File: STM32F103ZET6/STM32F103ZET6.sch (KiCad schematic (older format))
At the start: 74 parts, among them IC1 74HC1G66GW, J1 Conn_01x02, J2 Jack-DC, J3 +5V, J6 USB_B_Micro, Q1 S8050, Q2 S8550, SW1 RESET, SW2 SW_DIP_x01, U1 STM32F103ZETx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

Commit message: STM32F103ZET6.sch
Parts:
- added R14: 10k, symbol Device:R
- C31: value C -> 104
- R12, R13: renamed from R?; value R -> 10k
- U1: value STM32F103ZETx -> STM32F103ZET6
- gave numbers to parts that had none: 2
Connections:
- wire segments 243 -> 246
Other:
- note added: "SWD\n"
- note removed: "STLink"
- moved on the sheet: 1M1, C1, C2, C26, C27, C28, C29, C3, C30, C31, C32, C4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

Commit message: update
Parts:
- added D6, D7: LED, symbol Device:LED
- added R15, R16: 1k, symbol Device:R
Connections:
- net labels added: PB5, PE5
- wire segments 246 -> 255
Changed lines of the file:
@@
 Wire Notes Line
 	18500 4850 18500 500
+$Comp
+L Device:LED D7
+U 1 1 5E75F3EE
+P 14450 5700
+F 0 "D7" H 14443 5916 50  0000 C CNN
+F 1 "LED" H 14443 5825 50  0000 C CNN
+F 2 "" H 14450 5700 50  0001 C CNN
+F 3 "~" H 14450 5700 50  0001 C CNN
+	1    14450 5700
+	1    0    0    -1
+$EndComp
+$Comp
+L Device:LED D6
+U 1 1 5E75ECD8
+P 14450 5300
+F 0 "D6" H 14443 5516 50  0000 C CNN
+F 1 "LED" H 14443 5425 50  0000 C CNN
+F 2 "" H 14450 5300 50  0001 C CNN
+F 3 "~" H 14450 5300 50  0001 C CNN
+	1    14450 5300
+	1    0    0    -1
+$EndComp
+Text Label 14900 5500 0    50   ~ 0
+VCC_3V3
+$Comp
+L Device:R R15
+U 1 1 5E8949B0
+P 13950 5300
+F 0 "R15" V 13743 5300 50  0000 C CNN
+F 1 "1k" V 13834 5300 50  0000 C CNN
+F 2 "" V 13880 5300 50  0001 C CNN
+F 3 "~" H 13950 5300 50  0001 C CNN
+	1    13950 5300
+	0    1    1    0
+$EndComp
+$Comp
+L Device:R R16
+U 1 1 5E8957D1
+P 13950 5700
+F 0 "R16" V 13743 5700 50  0000 C CNN
+F 1 "1k" V 13834 5700 50  0000 C CNN
+F 2 "" V 13880 5700 50  0001 C CNN
+F 3 "~" H 13950 5700 50  0001 C CNN
+	1    13950 5700
+	0    1    1    0
+$EndComp
+Wire Wire Line
+	13800 5300 13600 5300
+Wire Wire Line
+	13800 5700 13600 5700
+Wire Wire Line
+	14100 5700 14300 5700
+Wire Wire Line
+	14100 5300 14300 5300
+Wire Wire Line
+	14600 5300 14700 5300
+Wire Wire Line
+	14700 5300 14700 5500
+Wire Wire Line
+	14700 5700 14600 5700
+Wire Wire Line
+	14700 5500 14900 5500
+Connection ~ 14700 5500
+Wire Wire Line
+	14700 5500 14700 5700
+Text Label 13600 5300 2    50   ~ 0
+PB5
+Text Label 13600 5700 2    50   ~ 0
+PE5
 Wire Bus Line
 	3600 800  3600 2000
@@
 Wire Bus Line
 	1500 3850 5850 3850
+Text Label 11000 6850 1    50   ~ 0
+PB5
+Text Label 14400 9450 3    50   ~ 0
+PE5
 $EndSCHEMATC

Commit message: add led & button
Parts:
- added SW3, SW4, SW5, SW6: SW_Push, symbol Switch:SW_Push
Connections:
- net labels added: +3.3V, PA0, PE2, PE3, PE4
- wire segments 255 -> 266
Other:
- note added: "Button\n"
- note added: "LED\n"
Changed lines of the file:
@@
 	16000 4050 16000 4200
-Wire Notes Line
-	500  6000 13000 6000
 Wire Notes Line
 	13000 500  13000 6000
@@
 Wire Wire Line
 	5350 5400 5500 5400
-Wire Notes Line
-	18500 4850 18500 500
 $Comp
 L Device:LED D7
@@
 Text Label 13600 5700 2    50   ~ 0
 PE5
+Text Label 11000 6850 1    50   ~ 0
+PB5
+Text Label 14400 9450 3    50   ~ 0
+PE5
+Wire Notes Line
+	15500 6000 15500 4850
+Text Notes 15200 5850 0    79   ~ 0
+LED\n
+$Comp
+L Switch:SW_Push SW5
+U 1 1 5E99870A
+P 16950 5500
+F 0 "SW5" V 16950 5750 50  0000 C CNN
+F 1 "SW_Push" V 16850 5700 50  0000 C CNN
+F 2 "" H 16950 5700 50  0001 C CNN
+F 3 "~" H 16950 5700 50  0001 C CNN
+	1    16950 5500
+	0    -1   -1   0
+$EndComp
+$Comp
+L Switch:SW_Push SW3
+U 1 1 5E9982B1
+P 16150 5500
+F 0 "SW3" V 16150 5750 50  0000 C CNN
+F 1 "SW_Push" V 16050 5750 50  0000 C CNN
+F 2 "" H 16150 5700 50  0001 C CNN
+F 3 "~" H 16150 5700 50  0001 C CNN
+	1    16150 5500
+	0    -1   -1   0
+$EndComp
+$Comp
+L Switch:SW_Push SW4
+U 1 1 5E99A749
+P 16550 5500
+F 0 "SW4" V 16550 5750 50  0000 C CNN
+F 1 "SW_Push" V 16450 5700 50  0000 C CNN
+F 2 "" H 16550 5700 50  0001 C CNN
+F 3 "~" H 16550 5700 50  0001 C CNN
+	1    16550 5500
+	0    -1   -1   0
+$EndComp
+$Comp
+L power:GND #PWR018
+U 1 1 5E9FC6A9
+P 16550 5100
+F 0 "#PWR018" H 16550 4850 50  0001 C CNN
+F 1 "GND" H 16450 5050 50  0000 R CNN
+F 2 "" H 16550 5100 50  0001 C CNN
+F 3 "" H 16550 5100 50  0001 C CNN
+	1    16550 5100
+	-1   0    0    1
+$EndComp
+Wire Wire Line
+	16150 5300 16150 5200
+Wire Wire Line
+	16150 5200 16550 5200
+Wire Wire Line
+	16950 5200 16950 5300
+Wire Wire Line
+	16550 5300 16550 5200
+Connection ~ 16550 5200
+Wire Wire Line
+	16550 5200 16950 5200
+Wire Wire Line
+	16550 5100 16550 5200
+Wire Wire Line
+	16150 5700 16150 5850
+Text Label 16150 5850 0    50   ~ 0
+PE2
+Wire Wire Line
+	16550 5700 16550 5850
+Text Label 16550 5850 0    50   ~ 0
+PE3
+Wire Wire Line
+	16950 5700 16950 5850
+Text Label 16950 5850 0    50   ~ 0
+PE4
+$Comp
+L Switch:SW_Push SW6
+U 1 1 5EB5954E
+P 17650 5500
+F 0 "SW6" H 17650 5785 50  0000 C CNN
+F 1 "SW_Push" H 17650 5694 50  0000 C CNN
+F 2 "" H 17650 5700 50  0001 C CNN
+F 3 "~" H 17650 5700 50  0001 C CNN
+	1    17650 5500
+	1    0    0    -1
+$EndComp
+$Comp
+L power:+3.3V #PWR019
+U 1 1 5EB5A9A3
+P 17900 5500
+F 0 "#PWR019" H 17900 5350 50  0001 C CNN
+F 1 "+3.3V" V 17915 5628 50  0000 L CNN
+F 2 "" H 17900 5500 50  0001 C CNN
+F 3 "" H 17900 5500 50  0001 C CNN
+	1    17900 5500
+	0    1    1    0
+$EndComp
+Wire Wire Line
+	17850 5500 17900 5500
+Text Label 17350 5500 2    50   ~ 0
+PA0
+Wire Wire Line
+	17350 5500 17450 5500
+Wire Notes Line
+	18500 500  18500 6000
+Wire Notes Line
+	500  6000 18500 6000
 Wire Bus Line
 	3600 800  3600 2000
@@
 Wire Bus Line
 	1500 3850 5850 3850
-Text Label 11000 6850 1    50   ~ 0
-PB5
-Text Label 14400 9450 3    50   ~ 0
-PE5
+Text Notes 17950 5900 0    79   ~ 0
+Button\n
 $EndSCHEMATC

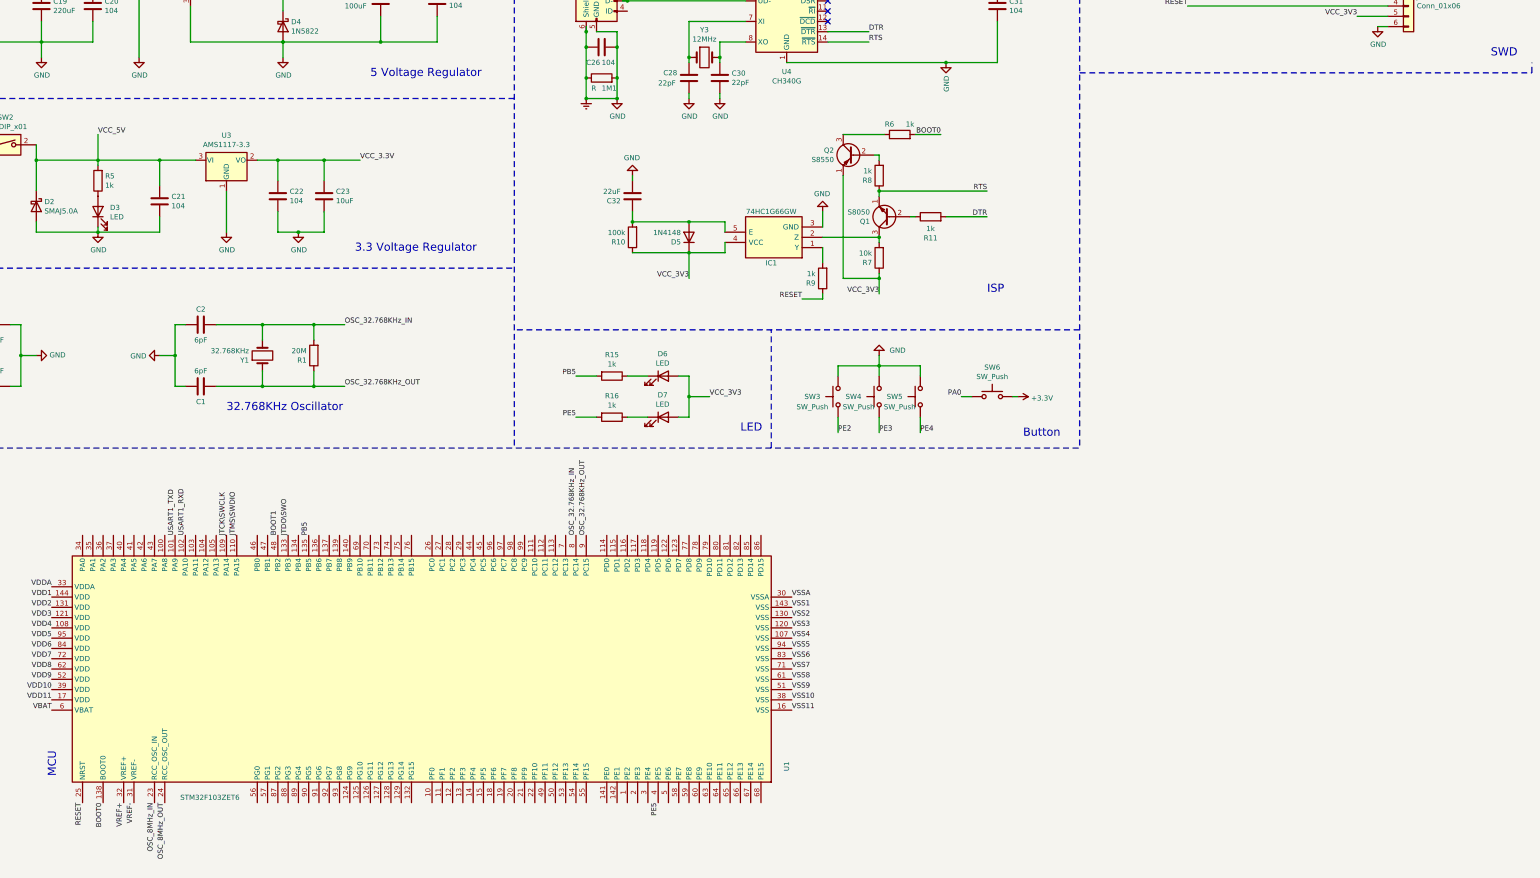
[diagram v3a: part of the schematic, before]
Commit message: add buzzer and DS18B20
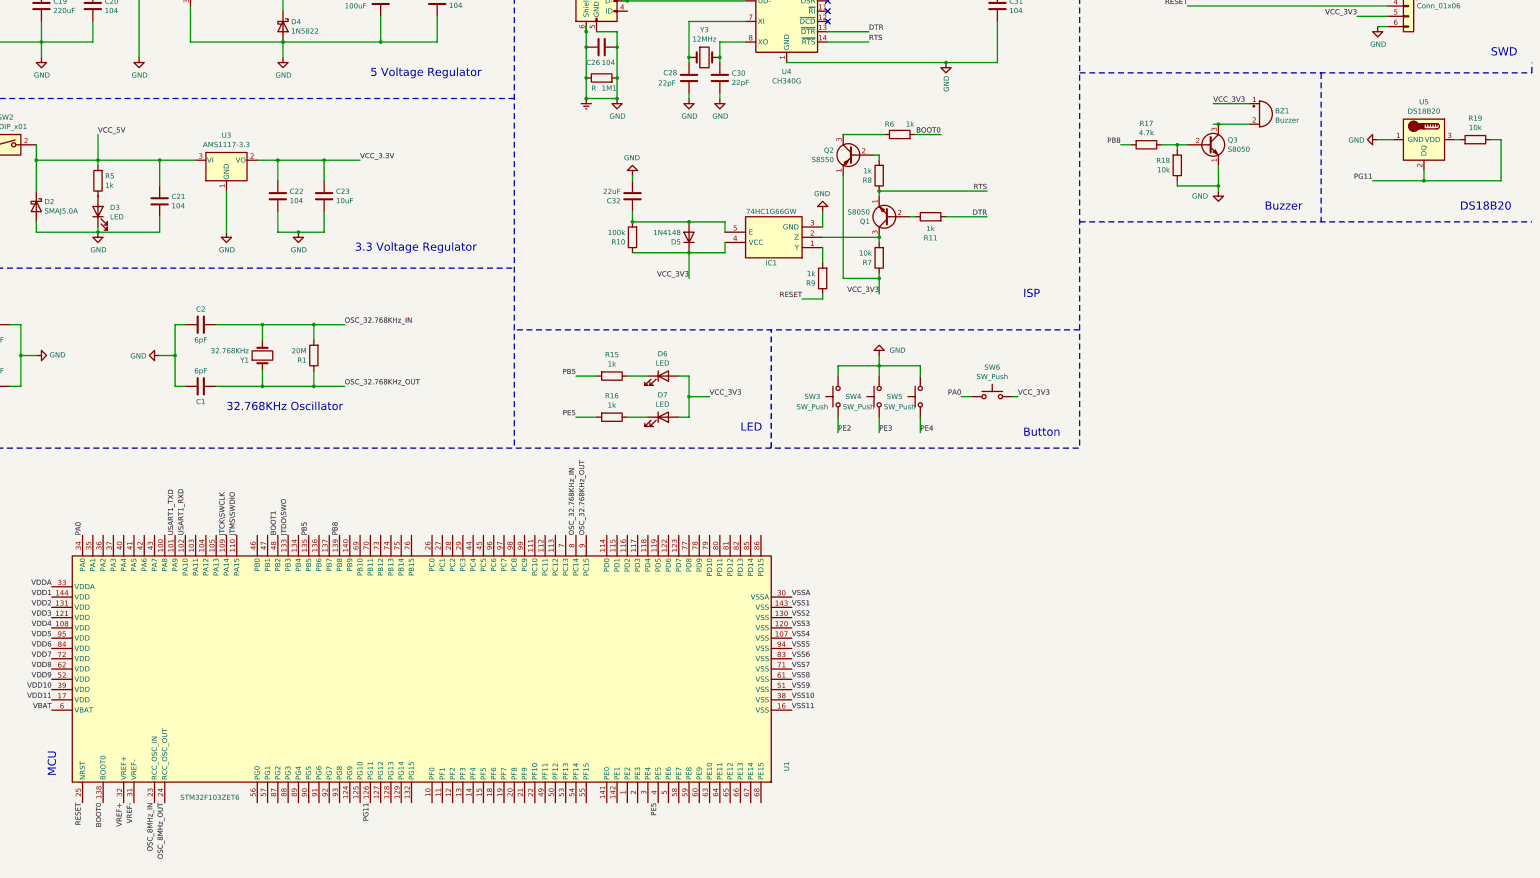
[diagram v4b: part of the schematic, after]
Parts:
- added BZ1: Buzzer, symbol Device:Buzzer
- added Q3: S8050, Package_TO_SOT_THT:TO-92_Inline, symbol Transistor_BJT:S8050
- added R17: 4.7k, symbol Device:R
- added R18, R19: 10k, symbol Device:R
- added U5: DS18B20, Package_TO_SOT_THT:TO-92_Inline, symbol Sensor_Temperature:DS18B20
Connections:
- net labels added: PB8, PG11
- net labels removed: +3.3V
- wire segments 266 -> 284
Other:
- note added: "Buzzer\n"
- note added: "DS18B20"
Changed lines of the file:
@@
 Wire Wire Line
 	17700 850  15550 850
-Text Notes 17600 4500 0    79   ~ 0
+Text Notes 17950 4550 0    79   ~ 0
 ISP
 $Comp
@@
 	1    0    0    -1
 $EndComp
-$Comp
-L power:+3.3V #PWR019
-U 1 1 5EB5A9A3
-P 17900 5500
-F 0 "#PWR019" H 17900 5350 50  0001 C CNN
-F 1 "+3.3V" V 17915 5628 50  0000 L CNN
-F 2 "" H 17900 5500 50  0001 C CNN
-F 3 "" H 17900 5500 50  0001 C CNN
-	1    17900 5500
-	0    1    1    0
-$EndComp
 Wire Wire Line
 	17850 5500 17900 5500
@@
 Wire Notes Line
 	500  6000 18500 6000
+Text Notes 17950 5900 0    79   ~ 0
+Button\n
+$Comp
+L Device:Buzzer BZ1
+U 1 1 5EC31AB9
+P 20250 2750
+F 0 "BZ1" H 20402 2779 50  0000 L CNN
+F 1 "Buzzer" H 20402 2688 50  0000 L CNN
+F 2 "" V 20225 2850 50  0001 C CNN
+F 3 "~" V 20225 2850 50  0001 C CNN
+	1    20250 2750
+	1    0    0    -1
+$EndComp
+Text Label 17900 5500 0    50   ~ 0
+VCC_3V3
+Text Label 8800 6850 1    50   ~ 0
+PA0
+$Comp
+L Transistor_BJT:S8050 Q3
+U 1 1 5EC560F5
+P 19750 3050
+F 0 "Q3" H 19940 3096 50  0000 L CNN
+F 1 "S8050" H 19940 3005 50  0000 L CNN
+F 2 "Package_TO_SOT_THT:TO-92_Inline" H 19950 2975 50  0001 L CIN
+F 3 "http://www.unisonic.com.tw/datasheet/S8050.pdf" H 19750 3050 50  0001 L CNN
+	1    19750 3050
+	1    0    0    -1
+$EndComp
+Text Label 19800 2650 0    50   ~ 0
+VCC_3V3
+Wire Wire Line
+	19800 2650 20150 2650
+Wire Wire Line
+	20150 2850 19850 2850
+$Comp
+L power:GND #PWR019
+U 1 1 5EC9C556
+P 19850 3500
+F 0 "#PWR019" H 19850 3250 50  0001 C CNN
+F 1 "GND" H 19750 3450 50  0000 R CNN
+F 2 "" H 19850 3500 50  0001 C CNN
+F 3 "" H 19850 3500 50  0001 C CNN
+	1    19850 3500
+	1    0    0    -1
+$EndComp
+$Comp
+L Device:R R17
+U 1 1 5ECAE34C
+P 19150 3050
+F 0 "R17" V 18943 3050 50  0000 C CNN
+F 1 "4.7k" V 19034 3050 50  0000 C CNN
+F 2 "" V 19080 3050 50  0001 C CNN
+F 3 "~" H 19150 3050 50  0001 C CNN
+	1    19150 3050
+	0    1    1    0
+$EndComp
+$Comp
+L Device:R R18
+U 1 1 5ECBFDD5
+P 19450 3250
+F 0 "R18" H 19380 3204 50  0000 R CNN
+F 1 "10k" H 19380 3295 50  0000 R CNN
+F 2 "" V 19380 3250 50  0001 C CNN
+F 3 "~" H 19450 3250 50  0001 C CNN
+	1    19450 3250
+	1    0    0    1
+$EndComp
+Wire Wire Line
+	19850 3250 19850 3450
+Wire Wire Line
+	19450 3050 19550 3050
+Connection ~ 19850 2850
+Wire Wire Line
+	19850 2850 19800 2850
+Wire Wire Line
+	19450 3450 19850 3450
+Wire Wire Line
+	19450 3400 19450 3450
+Wire Wire Line
+	19300 3050 19450 3050
+Connection ~ 19450 3050
+Wire Wire Line
+	19000 3050 18900 3050
+Text Label 18900 3050 2    50   ~ 0
+PB8
+Wire Wire Line
+	19450 3100 19450 3050
+Connection ~ 19850 3450
+Wire Wire Line
+	19850 3450 19850 3500
+Text Label 11300 6850 1    50   ~ 0
+PB8
+Wire Notes Line
+	18500 3800 22900 3800
+$Comp
+L Sensor_Temperature:DS18B20 U5
+U 1 1 5EF1BA85
+P 21850 3000
+F 0 "U5" V 21483 3000 50  0000 C CNN
+F 1 "DS18B20" V 21574 3000 50  0000 C CNN
+F 2 "Package_TO_SOT_THT:TO-92_Inline" H 20850 2750 50  0001 C CNN
+F 3 "http://datasheets.maximintegrated.com/en/ds/DS18B20.pdf" H 21700 3250 50  0001 C CNN
+	1    21850 3000
+	0    1    1    0
+$EndComp
+$Comp
+L Device:R R19
+U 1 1 5EF41527
+P 22350 3000
+F 0 "R19" V 22557 3000 50  0000 C CNN
+F 1 "10k" V 22466 3000 50  0000 C CNN
+F 2 "" V 22280 3000 50  0001 C CNN
+F 3 "~" H 22350 3000 50  0001 C CNN
+	1    22350 3000
+	0    1    -1   0
+$EndComp
+Wire Wire Line
+	22150 3000 22200 3000
+Wire Wire Line
+	22600 3000 22600 3400
+Wire Wire Line
+	21850 3400 21850 3300
+$Comp
+L power:GND #PWR020
+U 1 1 5EF9E7CC
+P 21400 3000
+F 0 "#PWR020" H 21400 2750 50  0001 C CNN
+F 1 "GND" V 21405 2872 50  0000 R CNN
+F 2 "" H 21400 3000 50  0001 C CNN
+F 3 "" H 21400 3000 50  0001 C CNN
+	1    21400 3000
+	0    1    1    0
+$EndComp
+Wire Wire Line
+	21400 3000 21550 3000
+Wire Wire Line
+	21850 3400 22600 3400
+Wire Wire Line
+	21850 3400 21350 3400
+Connection ~ 21850 3400
+Text Label 21350 3400 2    50   ~ 0
+PG11
+Wire Wire Line
+	22500 3000 22600 3000
+Wire Notes Line
+	20850 2350 20850 3800
 Wire Bus Line
 	3600 800  3600 2000
@@
 Wire Bus Line
 	1500 3850 5850 3850
-Text Notes 17950 5900 0    79   ~ 0
-Button\n
+Text Label 11600 9450 3    50   ~ 0
+PG11
+Text Notes 20300 3700 0    79   ~ 0
+Buzzer\n
+Text Notes 22200 3700 0    79   ~ 0
+DS18B20
 $EndSCHEMATC

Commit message: add sd card
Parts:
- added C33, C34: 104, symbol Device:C
- added J5, J7: Micro_SD_Card, symbol Connector:Micro_SD_Card
- added R20: 5.1m, symbol Device:R
- added U6: ESP8266EX, Package_DFN_QFN:QFN-32-1EP_5x5mm_P0.5mm_EP3.45x3.45mm, symbol MCU_Espressif:ESP8266EX
- added U7: W25Q32JVSS, Package_SO:SOIC-8_5.23x5.23mm_P1.27mm, symbol Memory_Flash:W25Q32JVSS
- added U8: NRF24L01, Package_DFN_QFN:QFN-20-1EP_4x4mm_P0.5mm_EP2.5x2.5mm, symbol RF:NRF24L01
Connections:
- net labels added: PA1, PB13, PB14, PB15, PC10, PC11, PC12, PC8, PC9, PD2
- wire segments 284 -> 316
- no-connect marks 5 -> 7
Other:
- note added: "SD(SDIO)\n"
- note added: "SD(SPI) / Touch Button\n\n"

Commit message: add EEPROM & SPI Flash
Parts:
- added C35: 104, symbol Device:C
- added R21, R22: 10k, symbol Device:R
- added U9: M24C02-WDW, Package_SO:TSSOP-8_4.4x3mm_P0.65mm, symbol Memory_EEPROM:M24C02-WDW
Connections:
- net labels added: PB10, PB11
- wire segments 316 -> 341
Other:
- note added: "2.4G\n"
- note added: "EEPROM\n"
- note added: "SPI Flash"
- note added: "WIFI"
- moved on the sheet: C34, J7, R20, U6, U7
